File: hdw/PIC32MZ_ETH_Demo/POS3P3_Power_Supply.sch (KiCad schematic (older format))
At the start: 11 parts

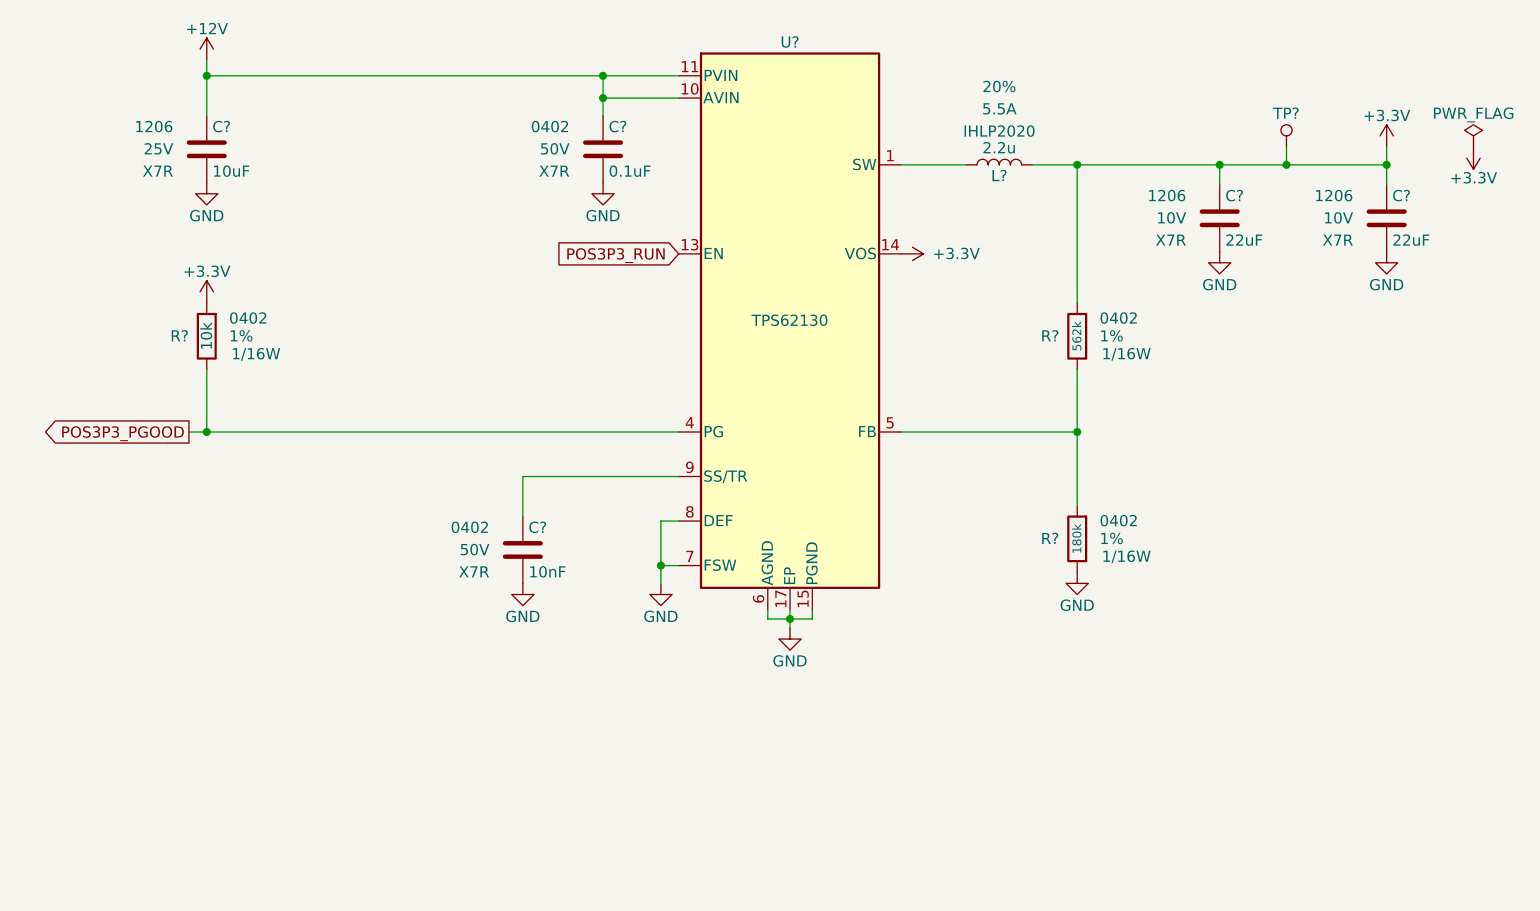
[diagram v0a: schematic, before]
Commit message: More schematic tweaks, followed PHY design guide
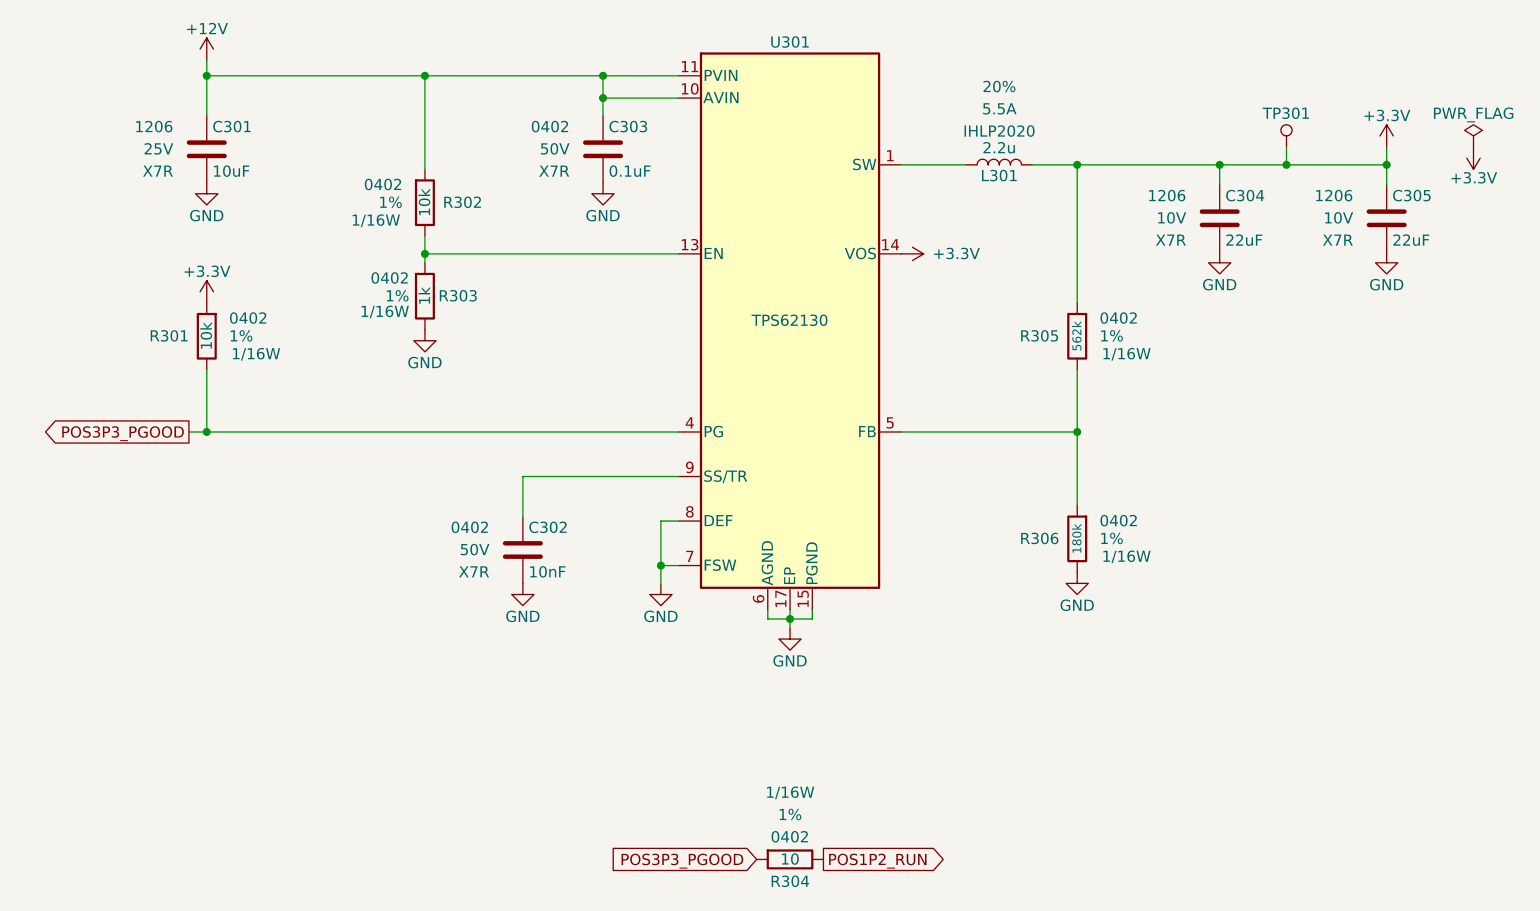
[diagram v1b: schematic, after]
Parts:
- added R302: 10k, Resistors_SMD:R_0402, symbol Custom_Library:R_Custom
- added R303: 1k, Resistors_SMD:R_0402, symbol Custom_Library:R_Custom
- added R304: 10, Resistors_SMD:R_0402, symbol Custom_Library:R_Custom
- gave numbers to parts that had none: 11
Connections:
- net +12V: now also R302.1
- net GND: now also R303.2
- net POS3P3_PGOOD: now also R304.1
- net POS3P3_RUN: no longer names the net of U301.13 (EN)
- net POS3P3_RUN: now also R302.2, R303.1
- new net POS1P2_RUN: R304.2

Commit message: Populated digi-key pn's
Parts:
- C302: Digi-Key PN (none) -> 490-13295-1-ND
- C303: Digi-Key PN (none) -> 490-10701-1-ND
- R301, R302: Digi-Key PN (none) -> RMCF0402FT10K0CT-ND
- R303: Digi-Key PN (none) -> 541-1.00KLCT-ND
- R304: Digi-Key PN (none) -> 541-3964-1-ND
- R305: Digi-Key PN (none) -> 541-562KLCT-ND
- R306: Digi-Key PN (none) -> 541-180KLCT-ND
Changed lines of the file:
@@
 F 5 "50V" H 3920 3250 50  0000 R CNN "Voltage"
 F 6 "X7R" H 3920 3150 50  0000 R CNN "Dielectric"
-F 7 "" H 4495 3750 60  0001 C CNN "Digi-Key PN"
+F 7 "490-10701-1-ND" H 4495 3750 60  0001 C CNN "Digi-Key PN"
 	1    4070 3250
 	1    0    0    -1
@@
 F 5 "1%" H 2390 4090 50  0000 L CNN "Tolerance"
 F 6 "1/16W" H 2400 4010 50  0000 L CNN "Wattage"
-F 7 "" H 2590 4490 60  0001 C CNN "Digi-Key PN"
+F 7 "RMCF0402FT10K0CT-ND" H 2590 4490 60  0001 C CNN "Digi-Key PN"
 	1    2290 4090
 	1    0    0    -1
@@
 F 5 "50V" H 3560 5050 50  0000 R CNN "Voltage"
 F 6 "X7R" H 3560 4950 50  0000 R CNN "Dielectric"
-F 7 "" H -210 830 50  0001 C CNN "Digi-Key PN"
+F 7 "490-13295-1-ND" H -210 830 50  0001 C CNN "Digi-Key PN"
 	1    3710 5050
 	1    0    0    -1
@@
 F 5 "1%" H 6300 4090 50  0000 L CNN "Tolerance"
 F 6 "1/16W" H 6310 4010 50  0000 L CNN "Wattage"
-F 7 "" H 6200 4090 50  0001 C CNN "Digi-Key PN"
+F 7 "541-562KLCT-ND" H 6200 4090 50  0001 C CNN "Digi-Key PN"
 	1    6200 4090
 	1    0    0    -1
@@
 F 5 "1%" H 6300 5000 50  0000 L CNN "Tolerance"
 F 6 "1/16W" H 6310 4920 50  0000 L CNN "Wattage"
-F 7 "" H 6200 5000 50  0001 C CNN "Digi-Key PN"
+F 7 "541-180KLCT-ND" H 6200 5000 50  0001 C CNN "Digi-Key PN"
 	1    6200 5000
 	1    0    0    -1
@@
 F 5 "1%" H 3370 3490 50  0000 L CNN "Tolerance"
 F 6 "1/16W" H 3380 3410 50  0000 L CNN "Wattage"
-F 7 "" H 3570 3890 60  0001 C CNN "Digi-Key PN"
+F 7 "RMCF0402FT10K0CT-ND" H 3570 3890 60  0001 C CNN "Digi-Key PN"
 	1    3270 3490
 	-1   0    0    -1
@@
 F 5 "1%" H 3340 3910 50  0000 L CNN "Tolerance"
 F 6 "1/16W" H 3340 3840 50  0000 L CNN "Wattage"
-F 7 "" H 3570 4310 60  0001 C CNN "Digi-Key PN"
+F 7 "541-1.00KLCT-ND" H 3570 4310 60  0001 C CNN "Digi-Key PN"
 	1    3270 3910
 	-1   0    0    -1
@@
 F 5 "1%" V 5110 6440 50  0000 C CNN "Tolerance"
 F 6 "1/16W" V 5210 6440 50  0000 C CNN "Wattage"
-F 7 "" H 5210 6840 60  0001 C CNN "Digi-Key PN"
+F 7 "541-3964-1-ND" H 5210 6840 60  0001 C CNN "Digi-Key PN"
 	1    4910 6440
 	0    -1   -1   0
